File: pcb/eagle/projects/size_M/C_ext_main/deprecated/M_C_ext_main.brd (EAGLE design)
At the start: 18 parts, among them U1 CP2104-F03-GM

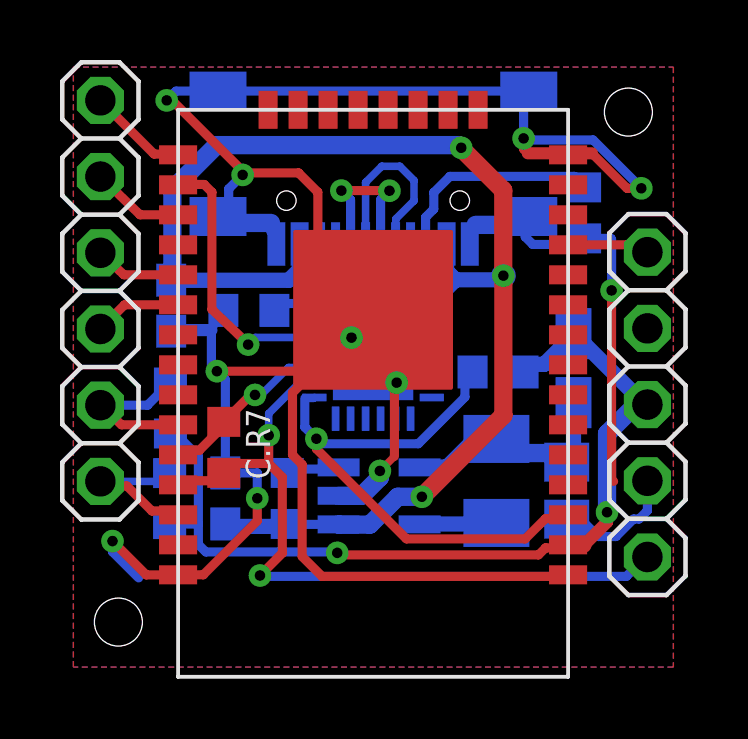
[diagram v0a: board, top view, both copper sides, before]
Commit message: version 8 main changes * ideal diode separated 3v3 DC-DC to protect it from back current * smaller package of ina 219 * usage of tssop attiny v2 in adapter * and change of PA5 to PB2 with ^ and ~ (originally used for shield power switch - now PB3) * step motor shield * out signal for BT module
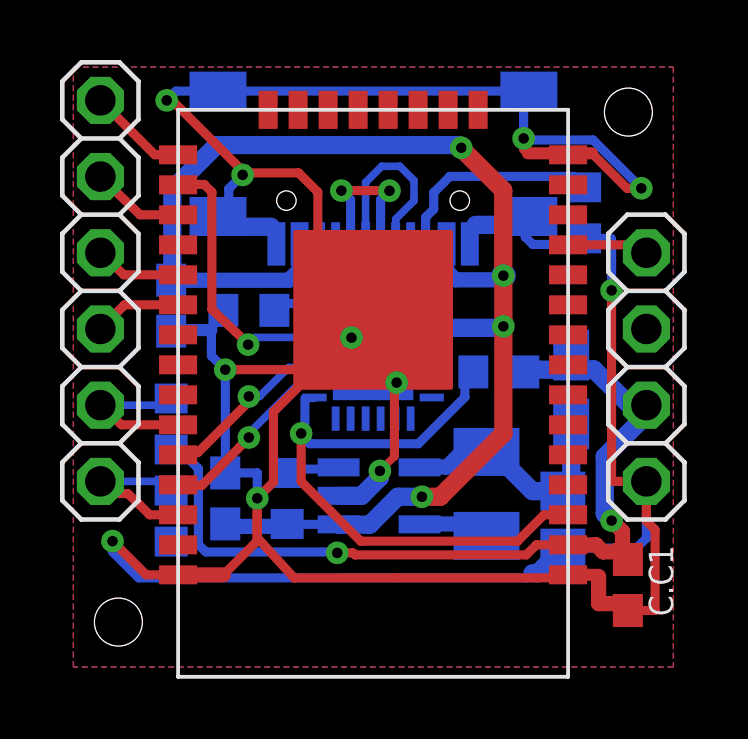
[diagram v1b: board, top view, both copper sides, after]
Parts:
- removed C.R7: 4k7, rcl:R0603
- removed JP2: (no value), pinhead2:1X05
- added C.C1: 100n, rcl:C0603
- added JP1: (no value), pinhead2:1X04
- moved C.C3 0.97 mm to (16.8, 5.42)
- moved C.D1 0.72 mm to (17.1, 9.75)
- moved C.R1 0.59 mm to (3.76, 5.53)
- moved D.L1 0.54 mm to (14.3, 6.27)
- moved C.R2 0.53 mm to (3.76, 8.60)
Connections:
- net GND: now also C.C1.2, JP1.4; no longer JP2.4
- net N$15: now also JP1.1; no longer JP2.1
- net RX: no longer C.R7.2, JP2.5
- net TX: no longer C.R7.1
- net VCC: now also C.C1.1, JP1.3; no longer JP2.3
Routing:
- net GND: track 122.7 -> 148.8 mm
- net RX: track 24.4 -> 6.06 mm, vias 2 -> 1
- net VCC: track 30.4 -> 32.5 mm
- net RESET: track 18.8 -> 20.5 mm
- net N$5: track 8.01 -> 8.90 mm
- net VUSB: track 44.8 -> 45.5 mm, vias 3 -> 4
